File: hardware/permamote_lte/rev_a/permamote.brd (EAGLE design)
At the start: 27 x 60 mm, 117 parts, among them IC1 NRF9160, J1 TC2030-JLINK-NL, J2 U.FL-R-SMT, J3 NANO_SIM, J4 U.FL-R-SMT, J5 DM3AT-SF-PEJM5, Q1 PMDXB950UPEL, Q10 PMDXB950UPEL, Q2 PMDXB950UPEL, Q3 PMDXB950UPEL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

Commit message: more routing fixes
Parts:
- moved J4 0.40 mm to (2.29, 50.8)
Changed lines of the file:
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@@
 <attribute name="NAME" x="6.731" y="52.197" size="1.016" layer="25" font="vector" ratio="12" rot="R90" align="bottom-center"/>
 </element>
-<element name="J4" library="connector" package="U.FL_SMT" value="U.FL-R-SMT" x="2.413" y="50.419" smashed="yes" rot="R90">
-<attribute name="DIGIKEY" value="H122041-ND" x="2.413" y="50.419" size="1.778" layer="27" rot="R90" display="off"/>
-<attribute name="MANUFACTURER" value="Hirose" x="2.413" y="50.419" size="1.778" layer="27" rot="R90" display="off"/>
-<attribute name="MPN" value="U.FL-R-SMT-1(01)" x="2.413" y="50.419" size="1.778" layer="27" rot="R90" display="off"/>
-<attribute name="NAME" x="-0.381" y="50.419" size="1.016" layer="25" font="vector" ratio="12" rot="R270" align="bottom-center"/>
+<element name="J4" library="connector" package="U.FL_SMT" value="U.FL-R-SMT" x="2.286" y="50.8" smashed="yes" rot="R90">
+<attribute name="DIGIKEY" value="H122041-ND" x="2.286" y="50.8" size="1.778" layer="27" rot="R90" display="off"/>
+<attribute name="MANUFACTURER" value="Hirose" x="2.286" y="50.8" size="1.778" layer="27" rot="R90" display="off"/>
+<attribute name="MPN" value="U.FL-R-SMT-1(01)" x="2.286" y="50.8" size="1.778" layer="27" rot="R90" display="off"/>
+<attribute name="NAME" x="-0.508" y="50.8" size="1.016" layer="25" font="vector" ratio="12" rot="R270" align="bottom-center"/>
 </element>
 <element name="ANT1" library="1462350001" package="ANT_1462350001" value="1462350001" x="2.286" y="56.896" smashed="yes" rot="R90">
@@
 <wire x1="6.966" y1="48.495" x2="6.985" y2="48.514" width="0.1524" layer="1" curve="-90"/>
 <wire x1="12.396" y1="57.041" x2="12.192" y2="57.245" width="0.1524" layer="16"/>
-<via x="0.635" y="47.625" extent="1-16" drill="0.2032"/>
+<via x="0.762" y="47.752" extent="1-16" drill="0.2032"/>
 <via x="5.334" y="48.514" extent="1-16" drill="0.2032"/>
 <via x="5.334" y="52.705" extent="1-16" drill="0.2032"/>
@@
 <polygon width="0.1524" layer="1">
 <vertex x="1.397" y="49.403"/>
-<vertex x="1.397" y="47.752"/>
-<vertex x="3.429" y="47.752"/>
+<vertex x="1.397" y="48.133"/>
+<vertex x="3.429" y="48.133"/>
 <vertex x="3.429" y="49.403"/>
 </polygon>
@@
 <via x="11.938" y="55.118" extent="1-16" drill="0.2032"/>
 <via x="12.319" y="59.309" extent="1-16" drill="0.2032"/>
-<wire x1="2.413" y1="51.894" x2="5.256" y2="51.894" width="0.1524" layer="1"/>
-<wire x1="5.256" y1="51.894" x2="5.334" y2="51.816" width="0.1524" layer="1"/>
+<wire x1="2.286" y1="52.275" x2="4.875" y2="52.275" width="0.1524" layer="1"/>
+<wire x1="4.875" y1="52.275" x2="5.334" y2="51.816" width="0.1524" layer="1"/>
 </signal>
 <signal name="VCC">
@@
 <wire x1="6.35" y1="52.14493125" x2="6.35" y2="51.36006875" width="0.1524" layer="1"/>
 <wire x1="6.35" y1="51.36006875" x2="6.126515625" y2="51.181" width="0.1524" layer="1"/>
-<wire x1="6.126515625" y1="51.181" x2="4.7" y2="51.181" width="0.1524" layer="1"/>
-<wire x1="4.7" y1="51.181" x2="3.938" y2="50.419" width="0.1524" layer="1"/>
+<wire x1="6.126515625" y1="51.181" x2="4.192" y2="51.181" width="0.1524" layer="1"/>
+<wire x1="4.192" y1="51.181" x2="3.811" y2="50.8" width="0.1524" layer="1"/>
 <wire x1="6.35" y1="51.36006875" x2="7.200503125" y2="51.36006875" width="0.1524" layer="1"/>
 <wire x1="7.18693125" y1="51.308" x2="7.200503125" y2="51.36006875" width="0.1524" layer="1"/>
@@
 <signal name="N$39">
 <polygon width="0.1524" layer="2" pour="cutout">
-<vertex x="4.826" y="48.133"/>
-<vertex x="0" y="48.133"/>
+<vertex x="4.826" y="48.387"/>
+<vertex x="0" y="48.387"/>
 <vertex x="0" y="53.213"/>
 <vertex x="4.826" y="53.213"/>
@@
 <signal name="N$43">
 <polygon width="0.1524" layer="15" pour="cutout">
-<vertex x="4.826" y="48.133"/>
-<vertex x="0" y="48.133"/>
+<vertex x="4.826" y="48.387"/>
+<vertex x="0" y="48.387"/>
 <vertex x="0" y="53.213"/>
 <vertex x="4.826" y="53.213"/>
@@
 <polygon width="0.1524" layer="16" pour="cutout">
 <vertex x="4.826" y="53.213"/>
-<vertex x="4.826" y="48.133"/>
-<vertex x="0" y="48.133"/>
+<vertex x="4.826" y="48.387"/>
+<vertex x="0" y="48.387"/>
 <vertex x="0" y="53.213"/>
 </polygon>

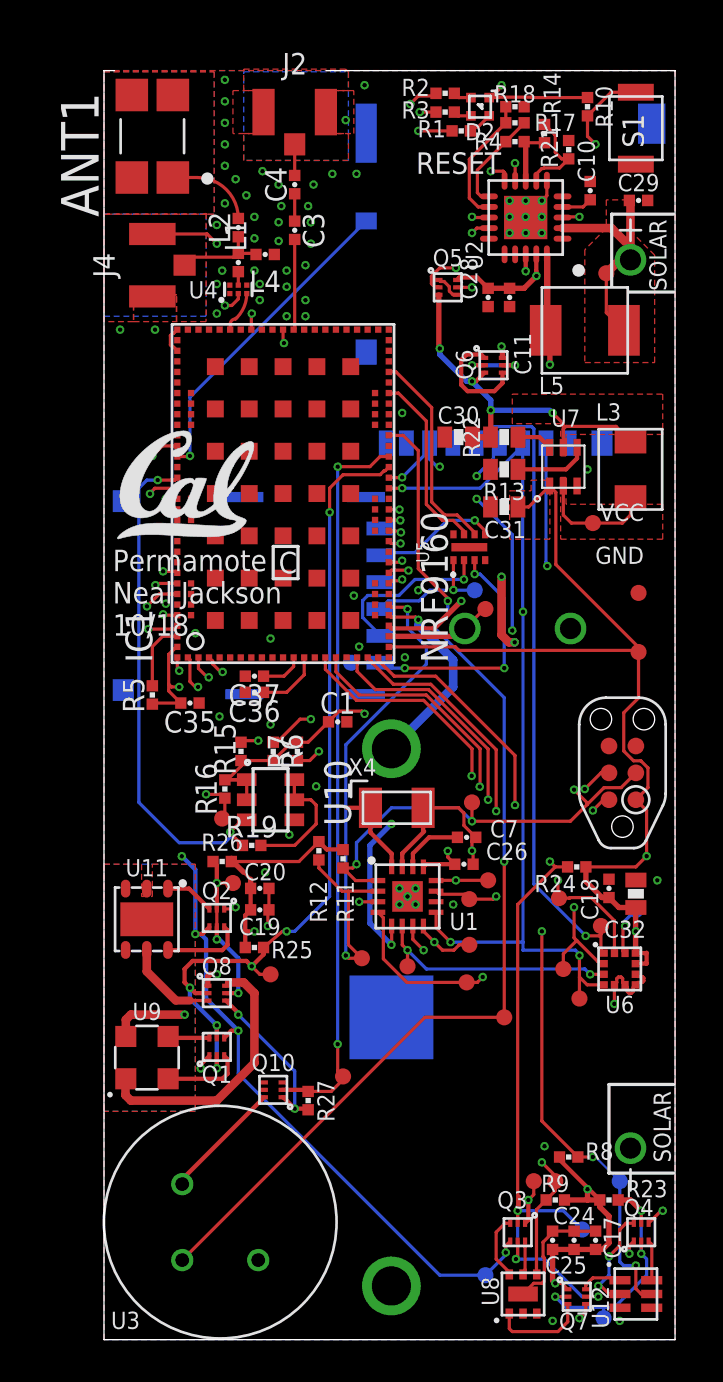
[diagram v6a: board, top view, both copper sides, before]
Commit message: made more changes but still having TPD3F303DPVR polygon issues
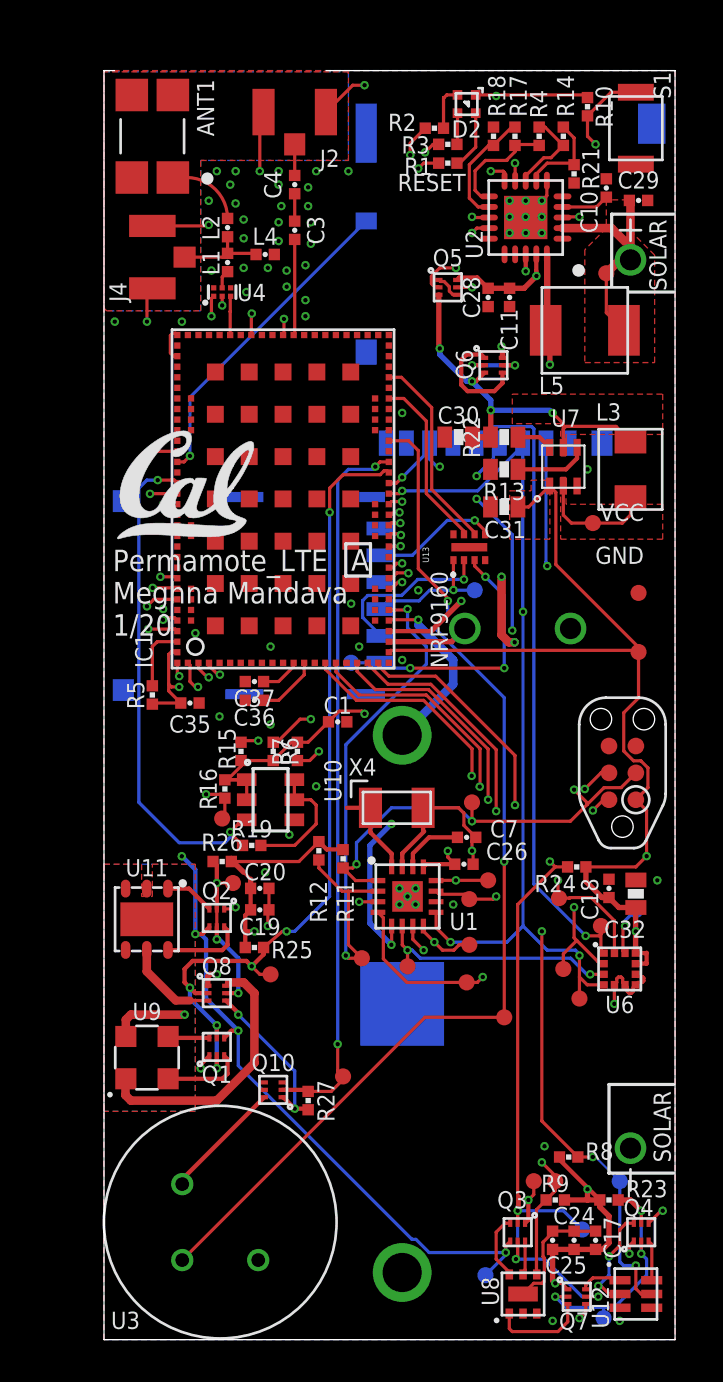
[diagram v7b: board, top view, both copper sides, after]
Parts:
- removed TP24: TEST-POINT, headers:PAD.03X.03
- moved R18 1.73 mm to (18.4, 56.9), turned to 270 degrees
- moved R2 1.73 mm to (15.6, 57.3)
- moved R1 1.65 mm to (16.3, 55.6)
- moved R3 1.53 mm to (16.3, 56.5)
- moved R21 1.17 mm to (22.2, 55.1), turned to 90 degrees
- moved R4 1.17 mm to (20.6, 56.9), turned to 90 degrees
- moved R14 0.90 mm to (21.7, 56.9)
- moved BAT1 0.81 mm to (14.1, 15.9)
- moved C10 0.77 mm to (23.7, 54.5)
- moved U4 0.77 mm to (5.59, 49.5)
- moved D2 0.65 mm to (17.1, 58.4)
- moved R17 0.63 mm to (19.4, 56.9), turned to 270 degrees
- moved L1 0.51 mm to (5.84, 50.9)
- moved L2 0.51 mm to (5.84, 52.6)
- moved C36 0.38 mm to (7.11, 30.2)
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- renumbered U5 to U13
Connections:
- removed net N$40: J3.C2
- net SIM_RST2: now also J3.C2
- net VSEC: no longer TP24.P$1
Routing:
- net GND: track 41.8 -> 50.5 mm, vias 75 -> 71
- net SIM_RST2: track 2.42 -> 6.26 mm
- net N$40: track 3.45 -> 0.00 mm
- net LED_RED: track 23.6 -> 21.4 mm
- net LED_GREEN: track 23.8 -> 21.7 mm
- net LED_BLUE: track 24.7 -> 22.8 mm
- net N$15: track 1.18 -> 2.80 mm
- net VBAT: track 66.4 -> 65.1 mm
- net N$17: track 0.87 -> 2.16 mm
- net N$32: track 2.84 -> 4.11 mm
- net VSEC: track 24.0 -> 22.7 mm
- net VCC: track 96.0 -> 95.0 mm
- net VREF_SAMP: track 1.45 -> 2.26 mm
- net N$58: track 4.84 -> 5.47 mm
- net N$19: track 0.86 -> 1.48 mm
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- removed copper zone on layer 1, net N$30
- removed copper zone on layer 2, net N$35
- removed copper zone on layer 15, net N$36
- removed copper zone on layer 16, net N$37
- removed copper zone on layer 1, net N$38
- removed copper zone on layer 2, net N$39
- removed copper zone on layer 15, net N$43
- removed copper zone on layer 16, net N$44
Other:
- board text added: "A"
- board text added: "Permamote_LTE Meghna Mandava 1/20"
- board text removed: ">REV"
- board text removed: "CR123A PACK -"
- board text removed: "Permamote Neal Jackson 10/18"

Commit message: before moving u10
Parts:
- moved TP27 3.91 mm to (26.2, 31.5)
- moved TP25 2.62 mm to (24.8, 40.6)
- moved C36 2.54 mm to (9.65, 30.2)
- moved C30 2.41 mm to (16.8, 45.1)
- moved L3 2.16 mm to (24.8, 43.3)
- moved R13 1.65 mm to (18.9, 42.8)
- moved TP26 1.45 mm to (24.9, 31.1)
- moved C37 1.40 mm to (8.51, 31.0)
- moved C31 1.40 mm to (18.9, 40.8)
- moved TP19 1.37 mm to (26.3, 19.6), flipped to the top
- moved R22 1.27 mm to (18.9, 43.9)
- moved J5 1.15 mm to (18.9, 43.4)
- moved Q6 1.14 mm to (18.4, 47.2)
- moved U7 1.02 mm to (21.7, 42.3)
- moved Q5 0.97 mm to (16.6, 50.6)
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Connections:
- removed net N$11: C4.2, J2.SIG
- removed net N$9: C3.1, IC1.ANT
- net GND: now also C3.1, C4.1, U1.5
- net N$8: now also C4.2, IC1.ANT, J2.SIG; no longer C4.1
- net VBAT: no longer U1.5
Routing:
- net VCC: track 95.0 -> 62.4 mm, vias 17 -> 21
- net !SD_DETECT: track 35.1 -> 17.7 mm, vias 2 -> 1
- net GND: track 50.5 -> 42.6 mm, vias 71 -> 90
- net N$8: track 1.29 -> 9.04 mm
- net N$45: track 1.26 -> 6.17 mm, vias 0 -> 2
- net N$9: track 4.54 -> 0.00 mm
- net MOSI: track 56.8 -> 59.2 mm
- net MISO: track 48.8 -> 51.0 mm
- net SCK: track 64.1 -> 65.9 mm
- net N$11: track 1.47 -> 0.00 mm
- net VOC_SAMP_VSTOR: track 10.5 -> 9.12 mm
- net LBST: track 5.42 -> 4.22 mm, vias 1 -> 0
- net N$13: track 29.6 -> 30.8 mm
- net !SD_CS: track 44.7 -> 45.9 mm
- net !VBAT_PRI_ON: track 14.3 -> 13.2 mm
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- added copper zone on layer 2, net N$11
- added copper zone on layer 15, net N$30
- added copper zone on layer 16, net N$35
- added copper zone on layer 16, net N$36
- added copper zone on layer 15, net N$37
- added copper zone on layer 2, net N$38
- added copper zone on layer 1, net N$39
- added copper zone on layer 1, net N$9
